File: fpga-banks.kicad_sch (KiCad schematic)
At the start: 9 parts, among them U2 ASFL1-100.000MHZ-L-T, U3 XC7K70T-FBG484

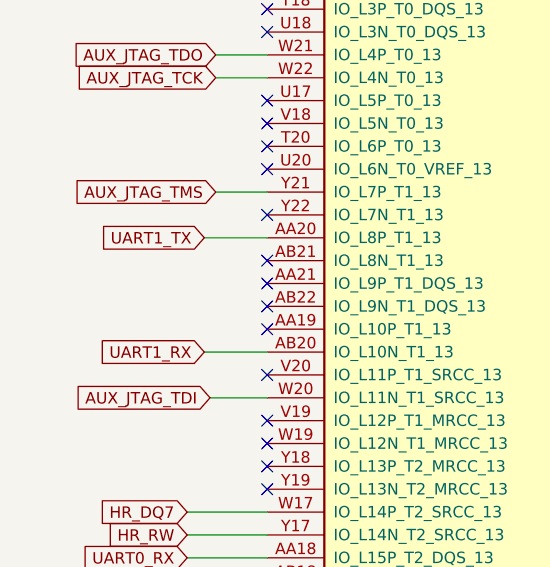
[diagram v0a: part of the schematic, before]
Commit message: Add DDR rail switches, update nets
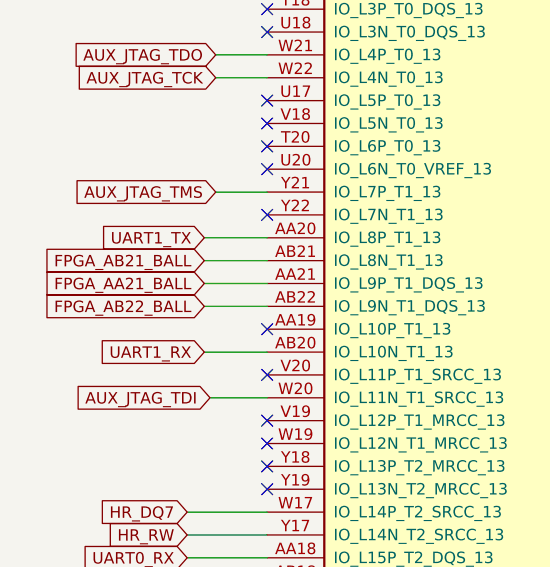
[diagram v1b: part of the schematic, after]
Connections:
- net FPGA_AA21_BALL: now reaches U3.AA21 (IO_L9P_T1_DQS_13)
- net FPGA_AB21_BALL: now reaches U3.AB21 (IO_L8N_T1_13)
- net FPGA_AB22_BALL: now reaches U3.AB22 (IO_L9N_T1_DQS_13)
- no-connect marks 32 -> 29
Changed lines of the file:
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@@
   (no_connect (at 121.92 160.02))
   (no_connect (at 121.92 58.42))
-  (no_connect (at 48.26 104.14))
   (no_connect (at 121.92 99.06))
-  (no_connect (at 48.26 99.06))
   (no_connect (at 48.26 63.5))
   (no_connect (at 48.26 111.76))
   (no_connect (at 48.26 60.96))
-  (no_connect (at 48.26 101.6))
   (no_connect (at 48.26 119.38))
   (no_connect (at 48.26 58.42))
@@
     (stroke (width 0) (type default) (color 0 0 0 0))
   )
+  (wire (pts (xy 41.275 99.06) (xy 48.26 99.06))
+    (stroke (width 0) (type default) (color 0 0 0 0))
+  )
   (wire (pts (xy 177.8 159.385) (xy 186.055 159.385))
     (stroke (width 0) (type default) (color 0 0 0 0))
@@
     (stroke (width 0) (type default) (color 0 0 0 0))
   )
+  (wire (pts (xy 41.275 104.14) (xy 48.26 104.14))
+    (stroke (width 0) (type default) (color 0 0 0 0))
+  )
   (wire (pts (xy 62.23 38.1) (xy 62.23 32.385))
     (stroke (width 0) (type default) (color 0 0 0 0))
@@
   )
   (wire (pts (xy 384.175 69.215) (xy 381 69.215))
+    (stroke (width 0) (type default) (color 0 0 0 0))
+  )
+  (wire (pts (xy 41.275 101.6) (xy 48.26 101.6))
     (stroke (width 0) (type default) (color 0 0 0 0))
   )
@@
     )
   )
+  (global_label "FPGA_AB21_BALL" (shape input) (at 41.275 99.06 180) (fields_autoplaced)
+    (effects (font (size 1.27 1.27)) (justify right))
+    (property "Intersheet References" "${INTERSHEET_REFS}" (id 0) (at 23.106 98.9806 0)
+      (effects (font (size 1.27 1.27)) (justify right) hide)
+    )
+  )
   (global_label "SD_DAT2" (shape input) (at 177.165 146.685 180) (fields_autoplaced)
     (effects (font (size 1.27 1.27)) (justify right))
@@
     )
   )
+  (global_label "FPGA_AA21_BALL" (shape input) (at 41.275 101.6 180) (fields_autoplaced)
+    (effects (font (size 1.27 1.27)) (justify right))
+    (property "Intersheet References" "${INTERSHEET_REFS}" (id 0) (at 23.2875 101.5206 0)
+      (effects (font (size 1.27 1.27)) (justify right) hide)
+    )
+  )
   (global_label "CK_TA" (shape input) (at 393.065 160.655 0) (fields_autoplaced)
     (effects (font (size 1.27 1.27)) (justify left))
@@
     )
   )
+  (global_label "FPGA_AB22_BALL" (shape input) (at 41.275 104.14 180) (fields_autoplaced)
+    (effects (font (size 1.27 1.27)) (justify right))
+    (property "Intersheet References" "${INTERSHEET_REFS}" (id 0) (at 23.106 104.0606 0)
+      (effects (font (size 1.27 1.27)) (justify right) hide)
+    )
+  )

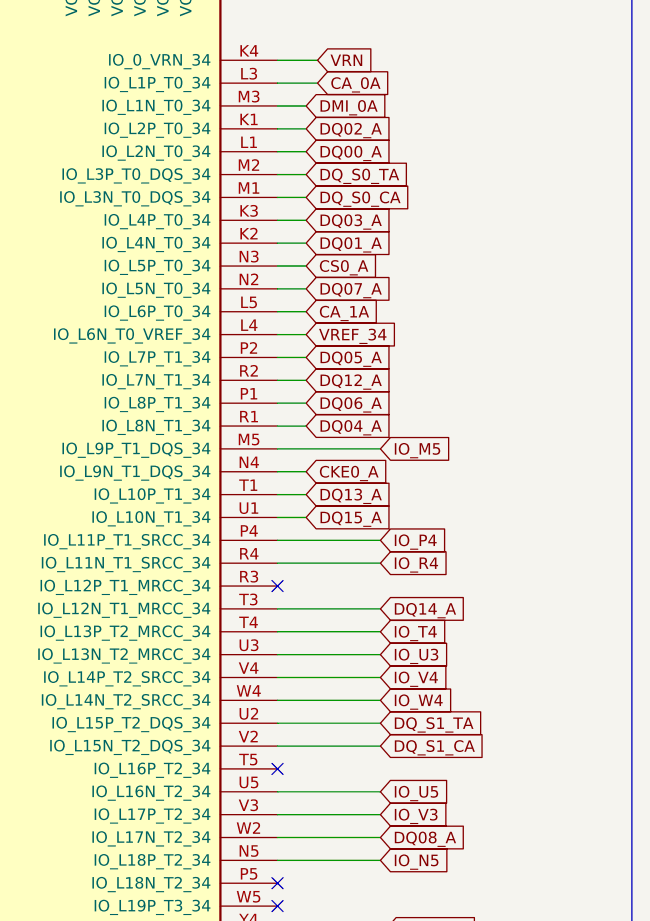
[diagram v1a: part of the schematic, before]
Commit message: DQS differential pairs renamed to be correctly recognized by KiCad, Created DQ and DQS class, DQ8-11 + DQ_S1 routed and matched with corrected class net parameters
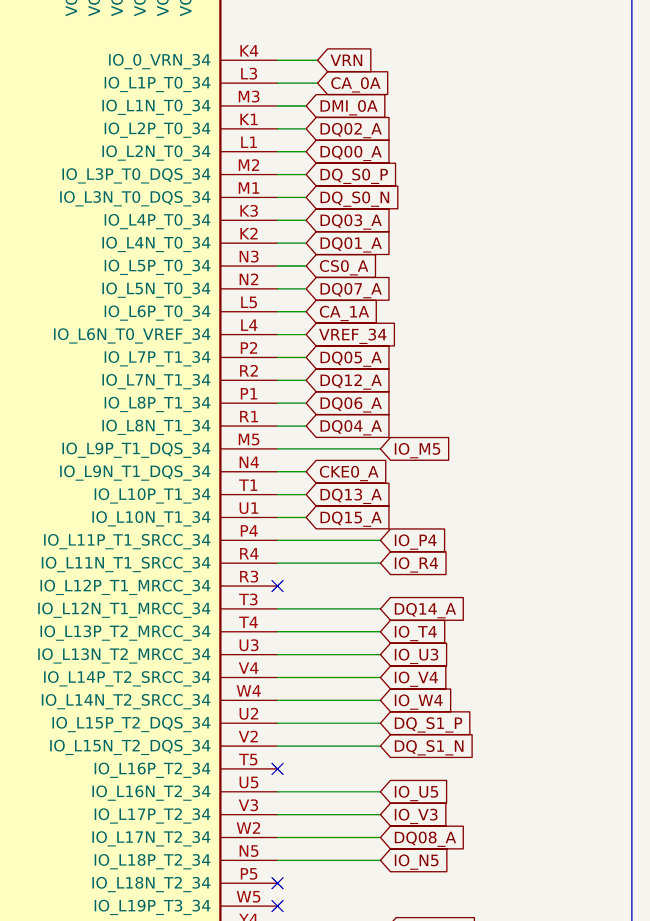
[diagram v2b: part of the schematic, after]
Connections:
- net DQ_S0_CA renamed DQ_S0_N
- net DQ_S0_TA renamed DQ_S0_P
- net DQ_S1_CA renamed DQ_S1_N
- net DQ_S1_TA renamed DQ_S1_P
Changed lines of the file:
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@@
     )
   )
-  (global_label "DQ_S0_TA" (shape input) (at 384.175 69.215 0) (fields_autoplaced)
-    (effects (font (size 1.27 1.27)) (justify left))
-    (property "Intersheet References" "${INTERSHEET_REFS}" (id 0) (at 0 0 0)
-      (effects (font (size 1.27 1.27)) hide)
-    )
-  )
-  (global_label "DQ_S1_TA" (shape input) (at 392.43 130.175 0) (fields_autoplaced)
-    (effects (font (size 1.27 1.27)) (justify left))
-    (property "Intersheet References" "${INTERSHEET_REFS}" (id 0) (at 0 0 0)
-      (effects (font (size 1.27 1.27)) hide)
+  (global_label "DQ_S0_P" (shape input) (at 384.175 69.215 0) (fields_autoplaced)
+    (effects (font (size 1.27 1.27)) (justify left))
+    (property "Intersheet References" "${INTERSHEET_REFS}" (id 0) (at 394.724 69.1356 0)
+      (effects (font (size 1.27 1.27)) (justify left) hide)
+    )
+  )
+  (global_label "DQ_S1_P" (shape input) (at 392.43 130.175 0) (fields_autoplaced)
+    (effects (font (size 1.27 1.27)) (justify left))
+    (property "Intersheet References" "${INTERSHEET_REFS}" (id 0) (at 402.979 130.0956 0)
+      (effects (font (size 1.27 1.27)) (justify left) hide)
     )
   )
@@
     )
   )
-  (global_label "DQ_S1_CA" (shape input) (at 392.43 132.715 0) (fields_autoplaced)
-    (effects (font (size 1.27 1.27)) (justify left))
-    (property "Intersheet References" "${INTERSHEET_REFS}" (id 0) (at 0 0 0)
-      (effects (font (size 1.27 1.27)) hide)
+  (global_label "DQ_S1_N" (shape input) (at 392.43 132.715 0) (fields_autoplaced)
+    (effects (font (size 1.27 1.27)) (justify left))
+    (property "Intersheet References" "${INTERSHEET_REFS}" (id 0) (at 403.0394 132.6356 0)
+      (effects (font (size 1.27 1.27)) (justify left) hide)
     )
   )
@@
     )
   )
-  (global_label "DQ_S0_CA" (shape input) (at 384.175 71.755 0) (fields_autoplaced)
-    (effects (font (size 1.27 1.27)) (justify left))
-    (property "Intersheet References" "${INTERSHEET_REFS}" (id 0) (at 0 0 0)
-      (effects (font (size 1.27 1.27)) hide)
-    )
-  )
+  (global_label "DQ_S0_N" (shape input) (at 384.175 71.755 0) (fields_autoplaced)
+    (effects (font (size 1.27 1.27)) (justify left))
+    (property "Intersheet References" "${INTERSHEET_REFS}" (id 0) (at 394.7844 71.6756 0)
+      (effects (font (size 1.27 1.27)) (justify left) hide)
+    )
+  )

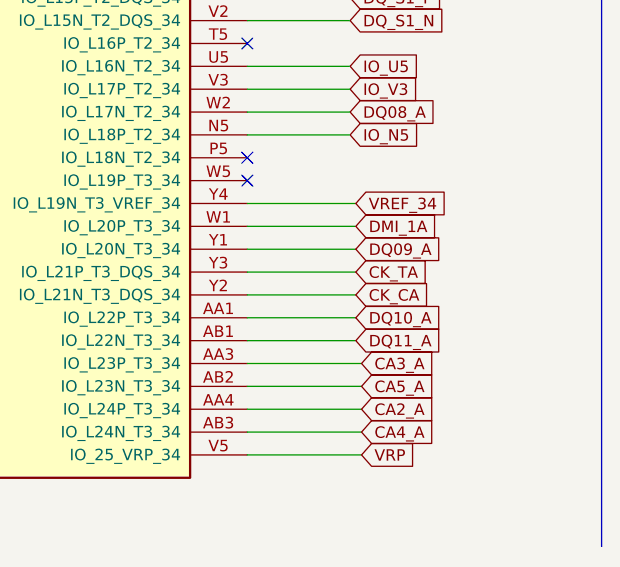
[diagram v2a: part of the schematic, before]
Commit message: Update name of CLK nets
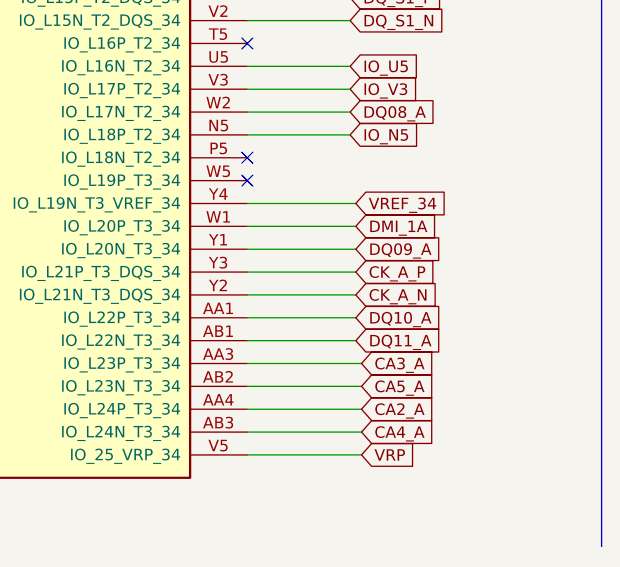
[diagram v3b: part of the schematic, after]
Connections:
- net CK_CA renamed CK_A_N
- net CK_TA renamed CK_A_P
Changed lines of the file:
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@@
-    )
-  )
-  (global_label "CK_CA" (shape input) (at 393.065 163.195 0) (fields_autoplaced)
-    (effects (font (size 1.27 1.27)) (justify left))
-    (property "Intersheet References" "${INTERSHEET_REFS}" (id 0) (at 0 0 0)
-      (effects (font (size 1.27 1.27)) hide)
     )
   )
@@
     (property "Intersheet References" "${INTERSHEET_REFS}" (id 0) (at 0 0 0)
       (effects (font (size 1.27 1.27)) hide)
+    )
+  )
+  (global_label "CK_A_N" (shape input) (at 393.065 163.195 0) (fields_autoplaced)
+    (effects (font (size 1.27 1.27)) (justify left))
+    (property "Intersheet References" "${INTERSHEET_REFS}" (id 0) (at 402.2835 163.1156 0)
+      (effects (font (size 1.27 1.27)) (justify left) hide)
     )
   )
@@
     )
   )
+  (global_label "CK_A_P" (shape input) (at 393.065 160.655 0) (fields_autoplaced)
+    (effects (font (size 1.27 1.27)) (justify left))
+    (property "Intersheet References" "${INTERSHEET_REFS}" (id 0) (at 402.223 160.5756 0)
+      (effects (font (size 1.27 1.27)) (justify left) hide)
+    )
+  )
   (global_label "VRN" (shape input) (at 385.445 56.515 0) (fields_autoplaced)
     (effects (font (size 1.27 1.27)) (justify left))
@@
     )
   )
-  (global_label "CK_TA" (shape input) (at 393.065 160.655 0) (fields_autoplaced)
-    (effects (font (size 1.27 1.27)) (justify left))
-    (property "Intersheet References" "${INTERSHEET_REFS}" (id 0) (at 0 0 0)
-      (effects (font (size 1.27 1.27)) hide)
-    )
-  )
